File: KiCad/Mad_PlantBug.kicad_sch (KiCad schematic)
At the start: 36 parts, among them IC1 TMP102AIDRLR, J1 SWD_Conn, Q1 NMOS, SW1 RST_Button, U1 YJ-14015, U2 TLV333IDBVR, U3 COMP

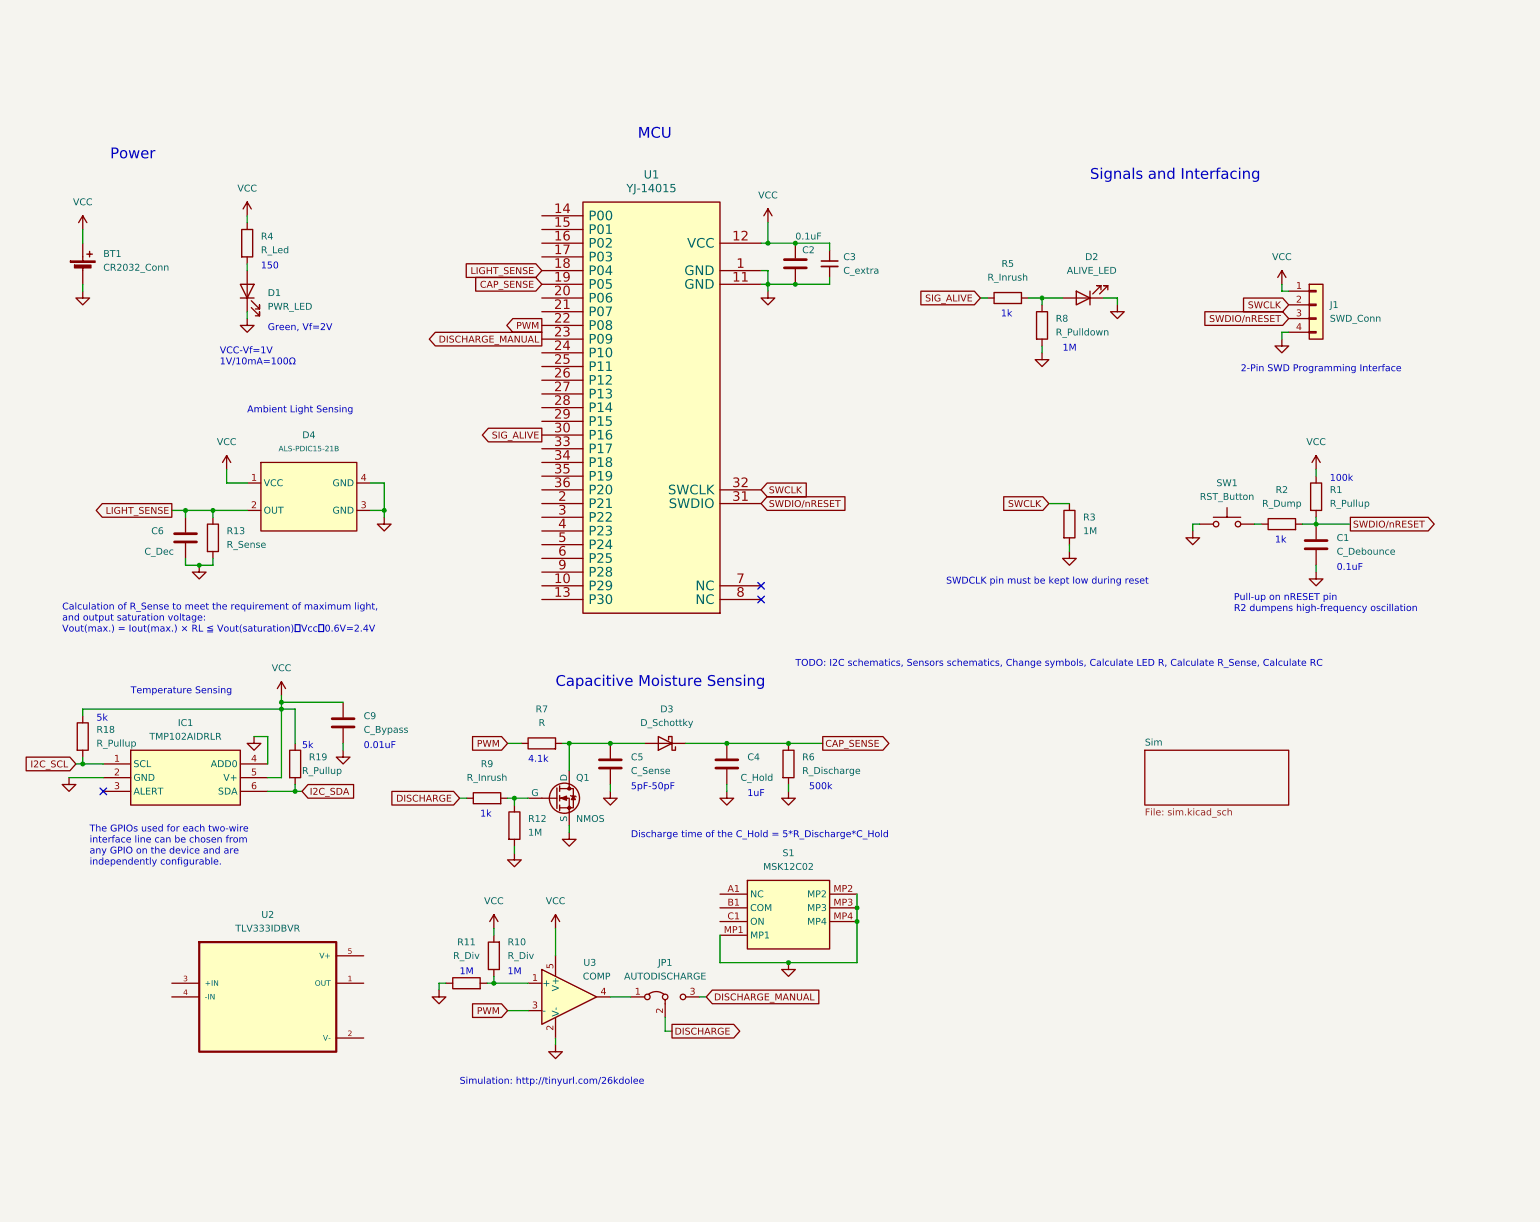
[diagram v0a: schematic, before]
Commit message: Last version of the full schematics with all assigned footprints. Added simulaion sheet.
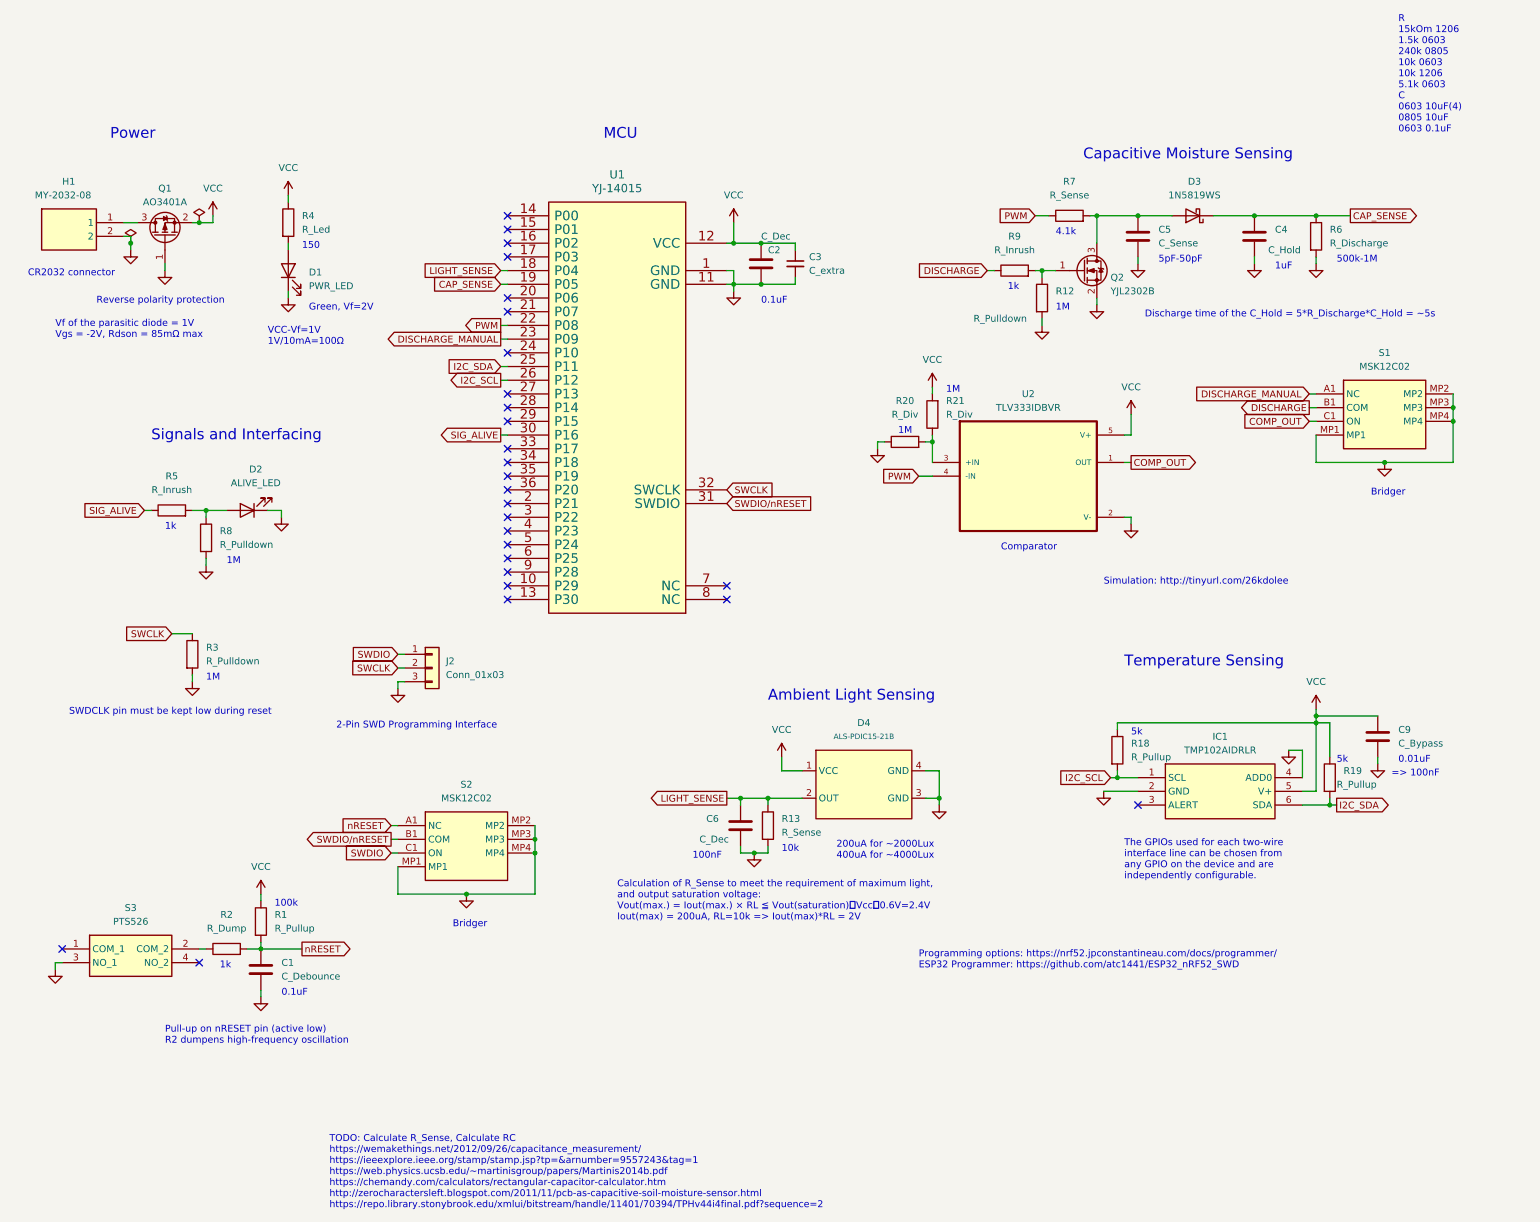
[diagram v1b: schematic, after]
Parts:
- removed BT1: CR2032_Conn, symbol Device:Battery_Cell
- removed J1: SWD_Conn, symbol Connector_Generic:Conn_01x04
- removed JP1: AUTODISCHARGE, Mad_PlantBug:MSK12C02, symbol Jumper:Jumper_3_Bridged12
- removed Q1: NMOS, Mad_PlantBug:ALS-PDIC15-21BTR8, symbol Simulation_SPICE:NMOS
- removed R10, R11: R_Div, symbol Device:R
- removed SW1: RST_Button, symbol Switch:SW_Push
- removed U3: COMP, Package_TO_SOT_SMD:SOT-23-5, symbol Amplifier_Operational:MCP6L01Ux-xOT
- added H1: MY-2032-08, Mad_PlantBug:MY203208, symbol Mad_PlantBug:MY-2032-08
- added J2: Conn_01x03, Mad_PlantBug:MOLEX_530480310, symbol Connector_Generic:Conn_01x03
- added Q1: AO3401A, Package_TO_SOT_SMD:SOT-23, symbol Transistor_FET:AO3401A
- added Q2: YJL2302B, Mad_PlantBug:SOT-23-3, symbol Device:Q_NMOS_GSD
- added R20, R21: R_Div, Resistor_SMD:R_0603_1608Metric_Pad0.98x0.95mm_HandSolder, symbol Device:R
- added S2: MSK12C02, Mad_PlantBug:MSK12C02, symbol Mad_PlantBug:MSK12C02
- added S3: PTS526, Mad_PlantBug:PTS526SK15SMTR2LFS, symbol Mad_PlantBug:PTS526_SK15_SMTR2_LFS
- C1, C3, C4, C6: footprint (none) -> Capacitor_SMD:C_0603_1608Metric
- C2: value 0.1uF -> C_Dec; footprint (none) -> Capacitor_SMD:C_0603_1608Metric_Pad1.08x0.95mm_HandSolder
- C9: footprint (none) -> Capacitor_SMD:C_0603_1608Metric_Pad1.08x0.95mm_HandSolder
- D1, D2: footprint (none) -> LED_SMD:LED_0603_1608Metric
- D3: value D_Schottky -> 1N5819WS; footprint (none) -> Mad_PlantBug:D_SOD-323_HandSoldering
- R1, R13, R18, R19, R5, R6, R8, R9: footprint (none) -> Resistor_SMD:R_0603_1608Metric_Pad0.98x0.95mm_HandSolder
- R12, R3: value 1M -> R_Pulldown; footprint (none) -> Resistor_SMD:R_0603_1608Metric_Pad0.98x0.95mm_HandSolder
- R2: footprint (none) -> Resistor_SMD:R_0402_1005Metric_Pad0.72x0.64mm_HandSolder
- R4: footprint (none) -> Resistor_SMD:R_0603_1608Metric
- R7: value R -> R_Sense; footprint (none) -> Resistor_SMD:R_0603_1608Metric_Pad0.98x0.95mm_HandSolder
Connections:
- net DISCHARGE: now also S1.B1 (COM)
- net DISCHARGE_MANUAL: now also S1.A1 (NC)
- net GND: now also U2.2 (V-), H1.2, J2.3 (Pin_3), Q1.1 (G), Q2.2 (S), R20.1, S2.MP1, S2.MP2, S2.MP3, S2.MP4, S3.3 (NO_1)
- net I2C_SCL: now also U1.26 (P12)
- net I2C_SDA: now also U1.25 (P11)
- net PWM: now also U2.4 (-IN)
- net SWCLK: now also J2.2 (Pin_2)
- net SWDIO/nRESET: now also S2.B1 (COM); no longer C1.1, R1.2, R2.2
- net VCC: now also U2.5 (V+), Q1.2 (S), R21.2
- net at R2.1: now also S3.2 (COM_2)
- net at C5.1, D3.2 (A), R7.2: now also Q2.3 (D)
- net COMP_OUT: now reaches S1.C1 (ON)
- net COMP_OUT: now also U2.1 (OUT)
- net at R12.1, R9.2: now also Q2.1 (G)
- net at U2.3 (+IN): now also R20.2, R21.1
- new net: H1.1, Q1.3 (D)
- new net SWDIO: J2.1 (Pin_1), S2.C1 (ON)
- new net nRESET: C1.1, R1.2, R2.2, S2.A1 (NC)
- no-connect marks 3 -> 27
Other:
- removed sheet Sim
- note added: "100nF"
- note added: "10k"
- note added: "200uA for ~2000Lux 400uA for ~4000Lux"
- note added: "500k-1M"
- note added: "=> 100nF"
- note added: "Bridger"
- note added: "CR2032 connector"
- note added: "Calculation of R_Sense to meet the requirement of maximum light, and output saturation voltage: Vout(max.) = Iout(max.) × RL ≦ Vout(saturation)＝Vcc－0.6V=2.4V Iout(max) = 200uA, RL=10k => Iout(max)*RL = 2V"
- note added: "Comparator"
- note added: "Discharge time of the C_Hold = 5*R_Discharge*C_Hold = ~5s"
- note added: "Programming options: https://nrf52.jpconstantineau.com/docs/programmer/ ESP32 Programmer: https://github.com/atc1441/ESP32_nRF52_SWD"
- note added: "Pull-up on nRESET pin (active low) R2 dumpens high-frequency oscillation"
- note added: "R 15kOm 1206 1.5k 0603 240k 0805 10k 0603 10k 1206 5.1k 0603 C 0603 10uF(4) 0805 10uF 0603 0.1uF"
- note added: "Reverse polarity protection"
- note added: "TODO: Calculate R_Sense, Calculate RC https://wemakethings.net/2012/09/26/capacitance_measurement/ https://ieeexplore.ieee.org/stamp/stamp.jsp?tp=&arnumber=9557243&tag=1 https://web.physics.ucsb.edu/~martinisgroup/papers/Martinis2014b.pdf https://chemandy.com/calculators/rectangular-capacitor-calculator.htm http://zerocharactersleft.blogspot.com/2011/11/pcb-as-capacitive-soil-moisture-sensor.html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"
- note added: "Vf of the parasitic diode = 1V Vgs = -2V, Rdson = 85mΩ max"
- note removed: "500k"
- note removed: "Calculation of R_Sense to meet the requirement of maximum light, and output saturation voltage: Vout(max.) = Iout(max.) × RL ≦ Vout(saturation)＝Vcc－0.6V=2.4V"
- note removed: "Discharge time of the C_Hold = 5*R_Discharge*C_Hold"
- note removed: "Pull-up on nRESET pin R2 dumpens high-frequency oscillation"
- note removed: "TODO: I2C schematics, Sensors schematics, Change symbols, Calculate LED R, Calculate R_Sense, Calculate RC"
- moved on the sheet: C1, C2, C3, C4, C5, C6, C9, D1, D2, D3, D4, IC1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

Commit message: Finished schematics, layed out the components, added ADC battery voltage input, defined board outline, traced a sensor capacitor.
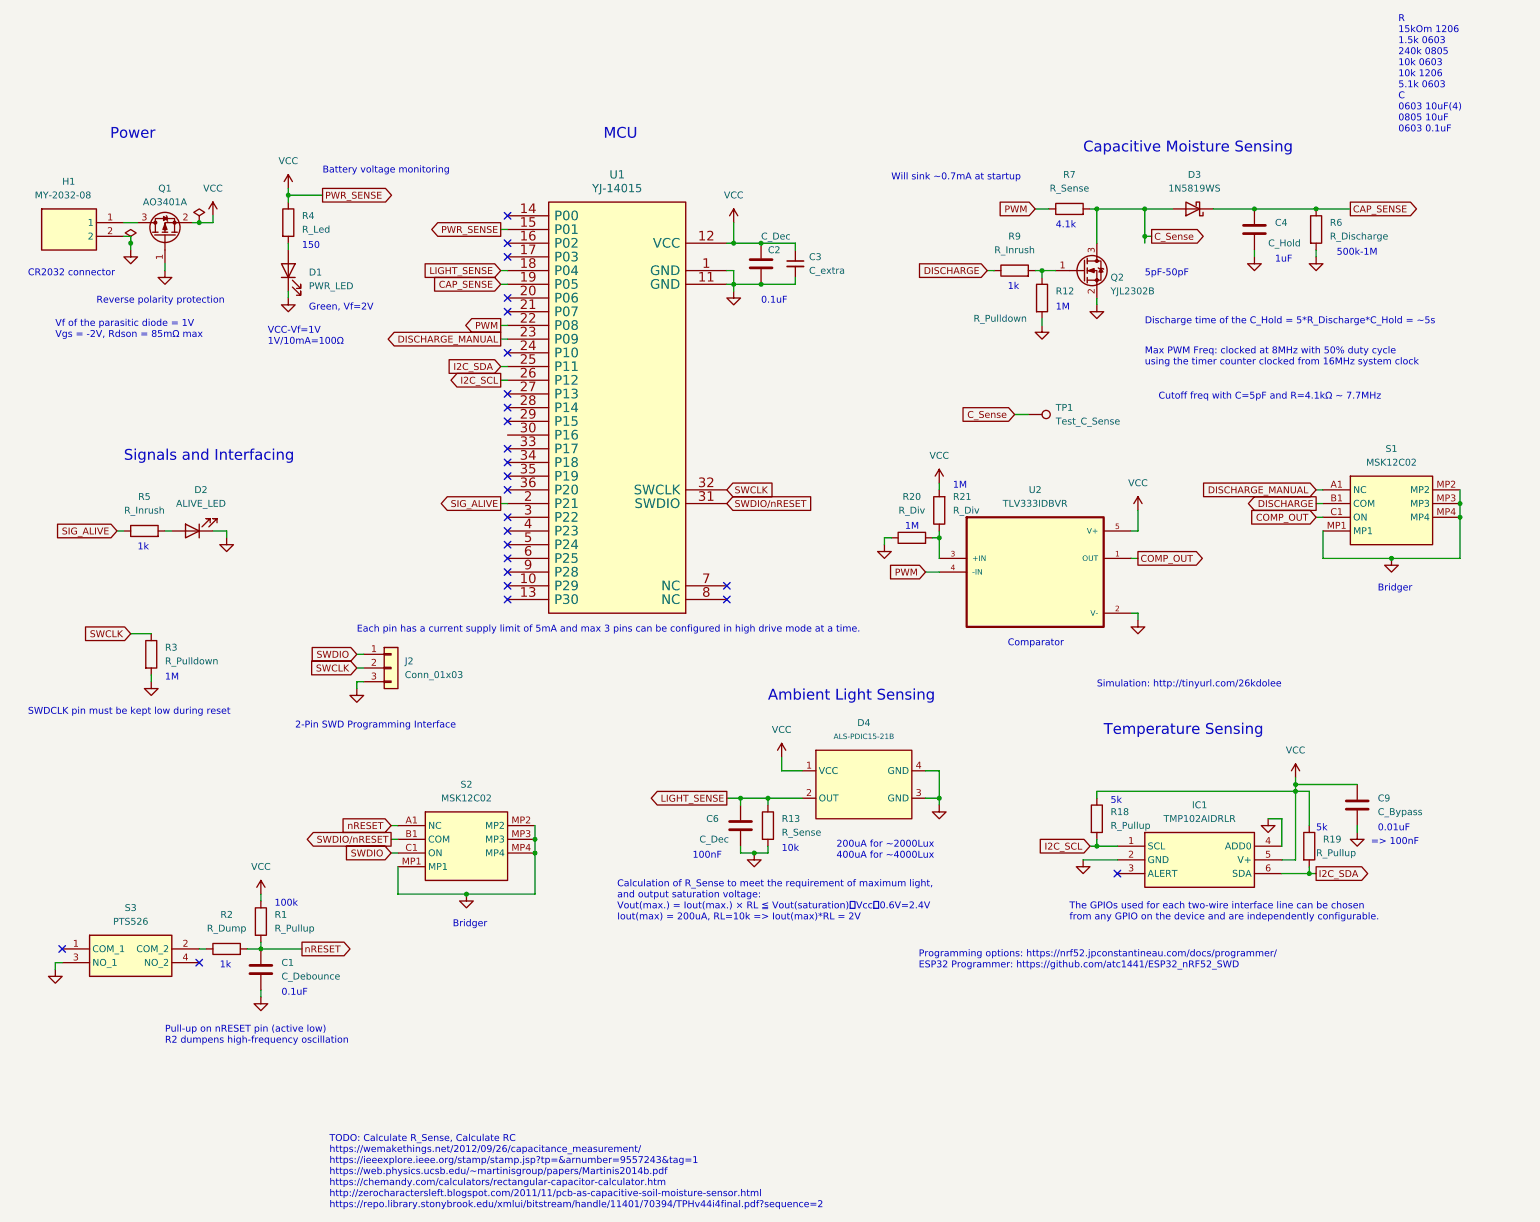
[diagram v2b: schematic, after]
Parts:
- removed C5: C_Sense, symbol Device:C
- removed R8: R_Pulldown, Resistor_SMD:R_0603_1608Metric_Pad0.98x0.95mm_HandSolder, symbol Device:R
- added TP1: Test_C_Sense, TestPoint:TestPoint_Pad_1.0x1.0mm, symbol Connector:TestPoint
- C3: footprint Capacitor_SMD:C_0603_1608Metric -> Capacitor_SMD:C_0402_1005Metric
- R1, R12, R13, R18, R19, R20, R21, R3, R5, R6, R9: footprint Resistor_SMD:R_0603_1608Metric_Pad0.98x0.95mm_HandSolder -> Resistor_SMD:R_0402_1005Metric_Pad0.72x0.64mm_HandSolder
- R4: footprint Resistor_SMD:R_0603_1608Metric -> Resistor_SMD:R_0402_1005Metric_Pad0.72x0.64mm_HandSolder
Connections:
- net SIG_ALIVE: now also U1.2 (P21); no longer U1.30 (P16)
- net VCC: now also U1.15 (P01)
- net C_Sense: now reaches D3.2 (A), Q2.3 (D), R7.2
- net C_Sense: now also TP1.1
- no-connect marks 27 -> 25
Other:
- note added: "Battery voltage monitoring"
- note added: "Cutoff freq with C=5pF and R=4.1kΩ ~ 7.7MHz"
- note added: "Each pin has a current supply limit of 5mA and max 3 pins can be configured in high drive mode at a time."
- note added: "Max PWM Freq: clocked at 8MHz with 50% duty cycle using the timer counter clocked from 16MHz system clock"
- note added: "Will sink ~0.7mA at startup"
- moved on the sheet: C4, C9, D2, D3, IC1, J2, R18, R19, R20, R21, R3, R5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
